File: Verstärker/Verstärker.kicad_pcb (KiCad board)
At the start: 2 copper layers, 99.5 x 53 mm, 63 parts, among them J3 ACJS-MHOM, J4 NRJ6HM-1, Q1 MJE182G, Q12 MMBT5401, Q12&Q13_E TP9, Q12_B TP4, Q12_C TP10, Q13 MMBT5401, Q13&Q12_C TP11, Q13_E TP8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

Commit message: Zweite Korrektur
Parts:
- moved Out 21.0 mm to (82.5, 63.5)
- moved Q12_B 10.8 mm to (78.5, 63.5)
- moved Q13_E 5.50 mm to (88.5, 63.5)
- moved C9 5.15 mm to (81.0, 70.0)
- moved Q12&Q13_E 4.00 mm to (74.5, 63.5)
- moved G*** 3.04 mm to (50.0, 71.0)
- moved Input 3.00 mm to (70.5, 63.5)
- moved Q2_E 2.83 mm to (119.0, 108.0)
- moved Q13&Q12_C 2.45 mm to (83.0, 107.0)
- moved R3 1.00 mm to (79.0, 78.0)
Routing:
- net Net-(D1-A): track 84.5 -> 111.0 mm
- net Net-(D2-K): track 32.8 -> 57.2 mm
- net Net-(Q2-E): track 33.3 -> 36.2 mm
- net Net-(D9-K): track 93.3 -> 90.5 mm
- net Net-(Q12-E): track 33.4 -> 34.6 mm
- net Net-(D2-A): track 35.9 -> 34.7 mm
- net Net-(D10-A): track 69.6 -> 68.6 mm

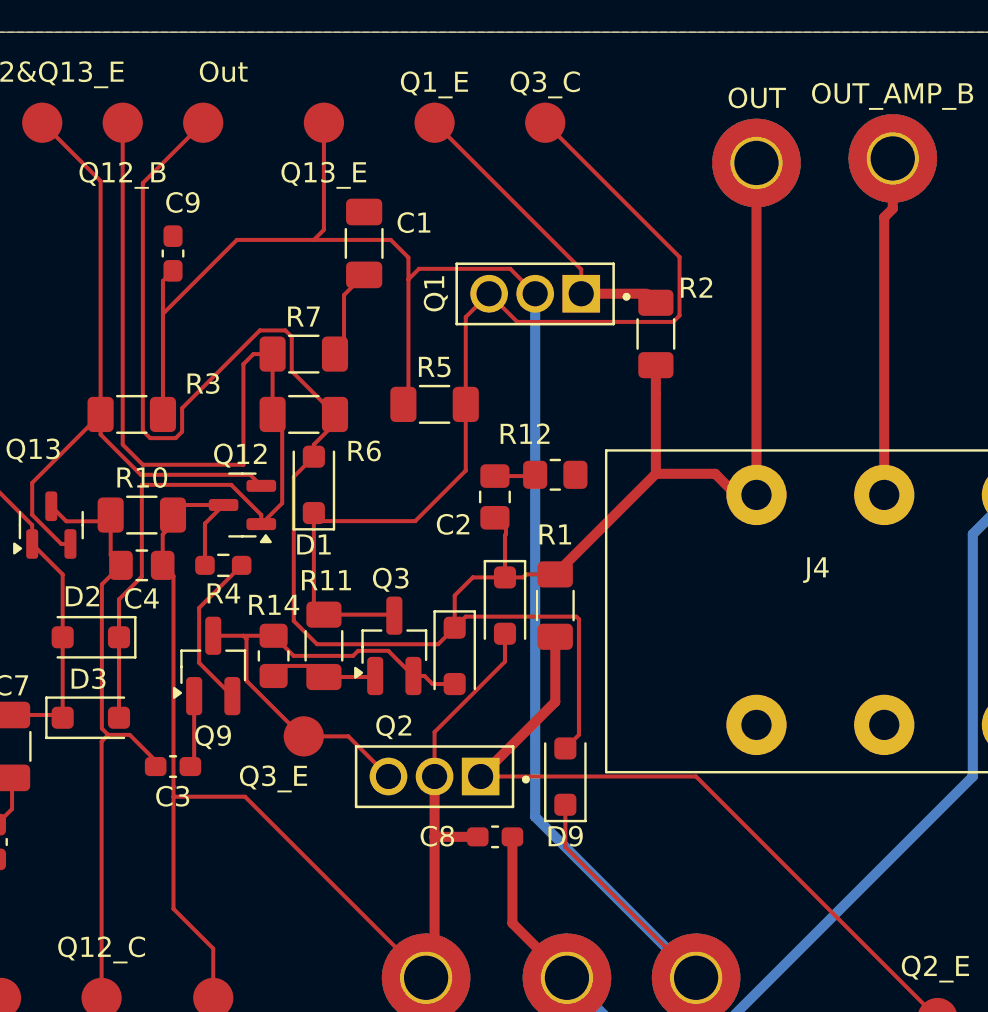
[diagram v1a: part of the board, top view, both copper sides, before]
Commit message: Testweise Produktionsdaten exportiert, muss später überschrieben werden. Fehler festgestellt in nicht vorhandenen JLCPCB Nummern.
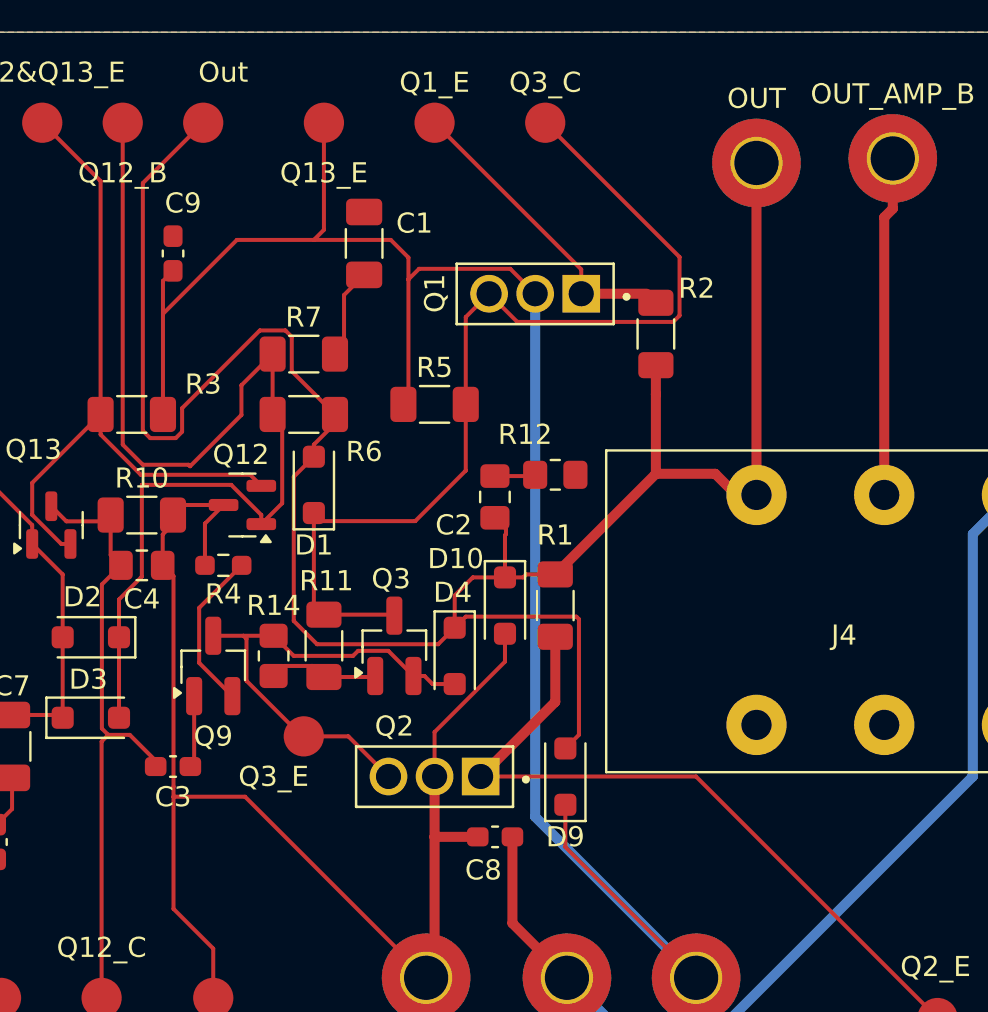
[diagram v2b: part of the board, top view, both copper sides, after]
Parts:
- J4: value NRJ6HM-1 -> ACJS-MHOM
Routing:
- net Net-(D2-K): track 57.2 -> 55.2 mm
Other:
- board text added: "D10"
- board text added: "D4"
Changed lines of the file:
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@@
 		(tags "neutrik jack slim")
 		(property "Reference" "J4"
-			(at 3.025 3.635 0)
+			(at 4.35 6.975 0)
 			(layer "F.SilkS")
 			(effects
@@
 			)
 		)
-		(property "Value" "NRJ6HM-1"
+		(property "Value" "ACJS-MHOM"
 			(at 6.35 15 0)
 			(layer "F.Fab")
@@
 		(tags "capacitor handsolder")
 		(property "Reference" "C1"
-			(at -1 -2.5 180)
+			(at -1 -2.5 0)
 			(layer "F.SilkS")
 			(effects
@@
 		(tags "capacitor handsolder")
 		(property "Reference" "C8"
-			(at 2.8625 0 180)
+			(at 0.5825 -1.655 180)
 			(layer "F.SilkS")
 			(effects
@@
 		)
 	)
+	(gr_text "D10"
+		(at 95.05 85.175 0)
+		(layer "F.SilkS")
+		(effects
+			(font
+				(size 1 1)
+				(thickness 0.15)
+			)
+		)
+	)
+	(gr_text "D4"
+		(at 94.9 86.85 0)
+		(layer "F.SilkS")
+		(effects
+			(font
+				(size 1 1)
+				(thickness 0.15)
+			)
+		)
+	)
 	(segment
 		(start 89.05 75)
@@
 	)
 	(segment
-		(start 78.5 79.5)
-		(end 78.5 63.5)
+		(start 86.426 82.4115)
+		(end 85.3875 83.45)
 		(width 0.2)
 		(layer "F.Cu")
@@
 	)
 	(segment
-		(start 86.426 82.4115)
-		(end 85.3875 83.45)
+		(start 84.4 78.025)
+		(end 84.4 76.55)
 		(width 0.2)
 		(layer "F.Cu")
@@
 	)
 	(segment
-		(start 84.5 75.5)
-		(end 84.5 80.5)
+		(start 81.85 80.575)
+		(end 84.4 78.025)
+		(width 0.2)
+		(layer "F.Cu")
+		(net 12)
+	)
+	(segment
+		(start 78.5 63.5)
+		(end 78.5 79.5)
 		(width 0.2)
 		(layer "F.Cu")
@@
 	)
 	(segment
-		(start 79.45 81.5)
-		(end 79.45 86.06116)
+		(start 79.5 80.5)
+		(end 81.775 80.5)
 		(width 0.2)
 		(layer "F.Cu")
@@
 	)
 	(segment
-		(start 85.95 75)
-		(end 85.95 78)
+		(start 79.45 81.5)
+		(end 79.45 86.06116)
 		(width 0.2)
 		(layer "F.Cu")
@@
 	(segment
 		(start 85.95 75)
-		(end 85 75)
+		(end 85.95 78)
 		(width 0.2)
 		(layer "F.Cu")
@@
 	)
 	(segment
-		(start 84.5 80.5)
-		(end 79.5 80.5)
+		(start 84.4 76.55)
+		(end 85.95 75)
 		(width 0.2)
 		(layer "F.Cu")
@@
 	)
 	(segment
-		(start 86.426 78.476)
-		(end 86.426 82.4115)
+		(start 78.5 79.5)
+		(end 79.5 80.5)
 		(width 0.2)
 		(layer "F.Cu")
@@
 	)
 	(segment
-		(start 85.3875 83.45)
-		(end 85.3875 82.995532)
+		(start 81.775 80.5)
+		(end 81.85 80.575)
 		(width 0.2)
 		(layer "F.Cu")
@@
 	)
 	(segment
-		(start 79.5 80.5)
-		(end 78.5 79.5)
+		(start 86.426 78.476)
+		(end 86.426 82.4115)
 		(width 0.2)
 		(layer "F.Cu")
@@
 	)
 	(segment
-		(start 85 75)
-		(end 84.5 75.5)
+		(start 85.3875 83.45)
+		(end 85.3875 82.995532)
 		(width 0.2)
 		(layer "F.Cu")
